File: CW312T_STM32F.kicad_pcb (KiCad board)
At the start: 2 copper layers, 58.7 x 53.7 mm, 24 parts, among them J1 HDR_6_2.54, P1 PCIEx4 EDGE CONNECTOR, U1 STM32F100RBT6B

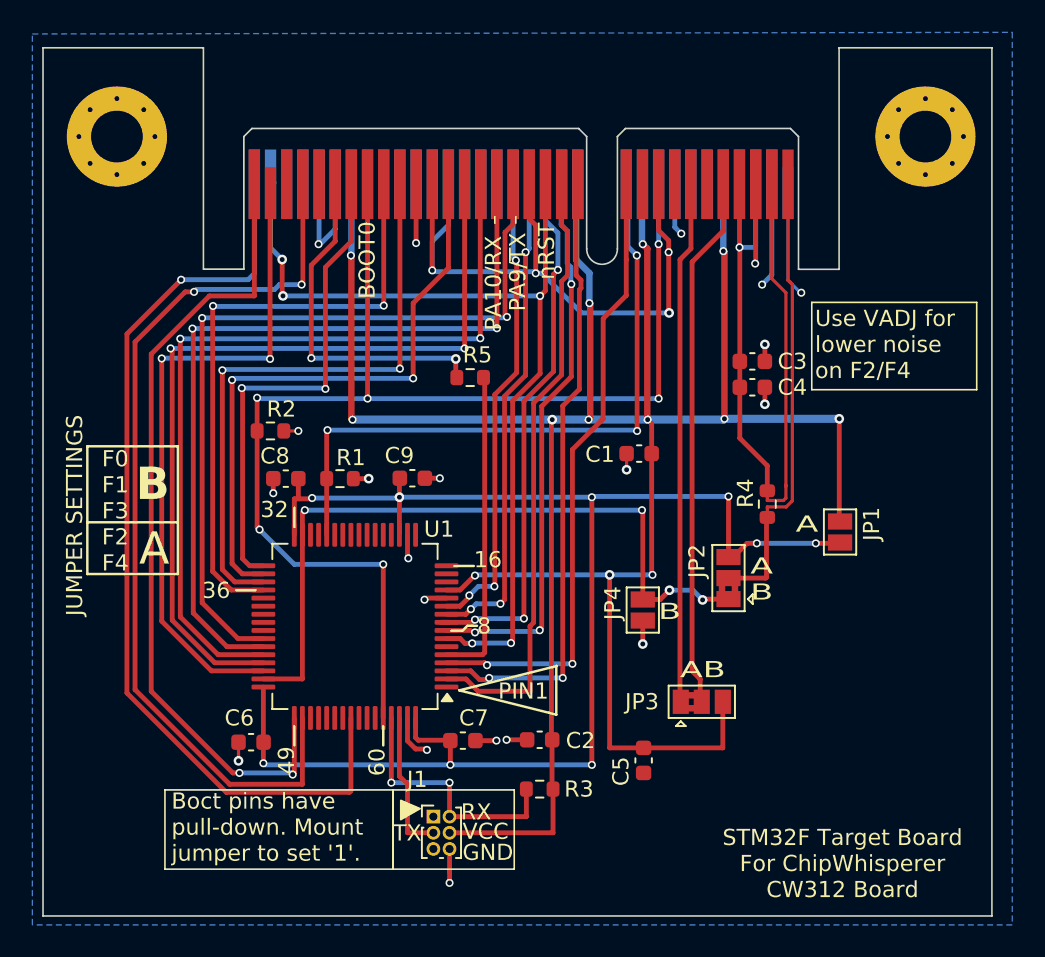
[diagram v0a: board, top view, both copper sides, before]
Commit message: updated design - fixed connections, got rid of visible pin numbers on passives, updated silkscreen
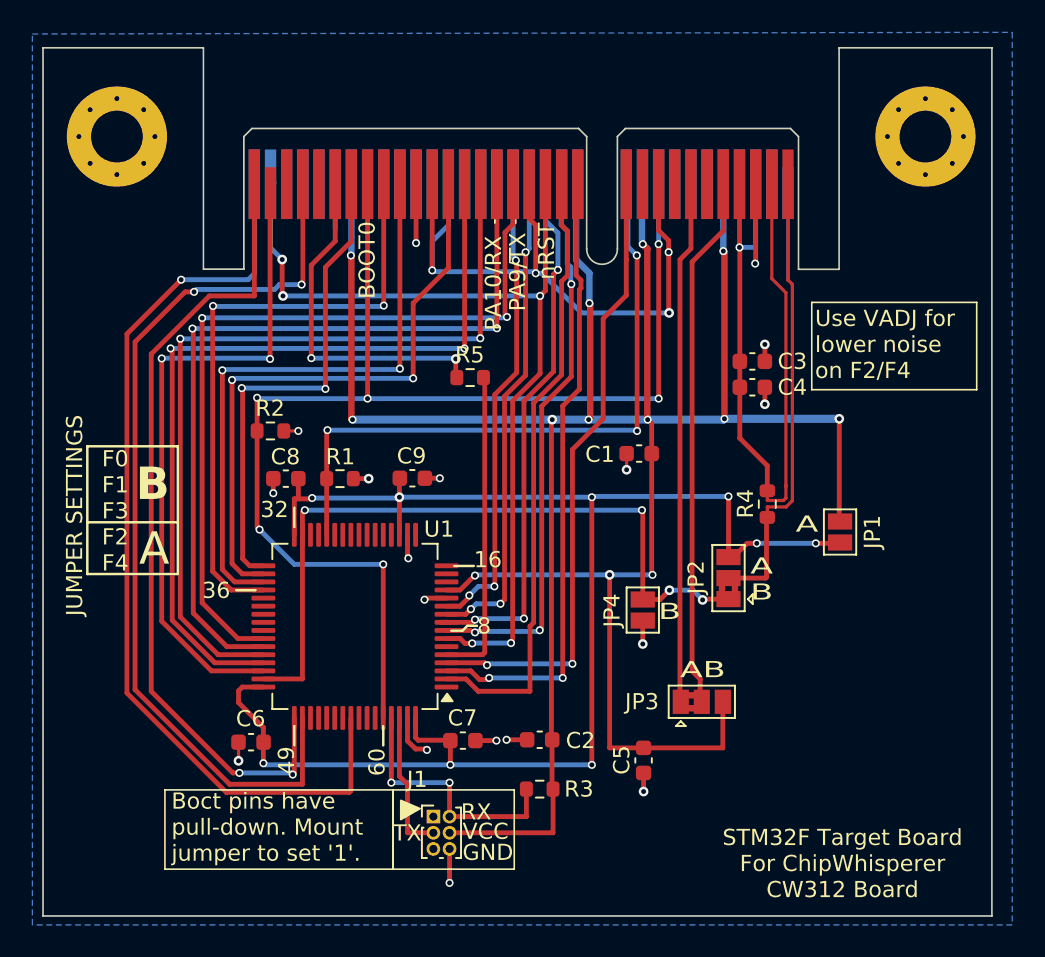
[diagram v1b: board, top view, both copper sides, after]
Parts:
- added PCB4: UKCA symbol, Silkscrren_Symbols:UKCA-Logo_8x8mm_SilkScreen, F.Cu at (135.1, 87.8)
- PCB2: footprint Silkscrren_Symbols:WEEE-Logo_8.4x12mm_SilkScreen -> Silkscrren_Symbols:WEEE-Logo_5.6x8mm_SilkScreen
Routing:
- net GND: track 93.3 -> 78.5 mm, vias 25 -> 22
- net Net-(U1B-VDD_1): track 91.3 -> 93.4 mm
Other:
- board text removed: "PIN1"
